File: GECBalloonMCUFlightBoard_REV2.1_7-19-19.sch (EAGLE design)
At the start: 59 parts, among them IC1 PIC32MX360F512L, Q1 IRF3704L-V, Q2 IRF3704L-V, U1 ADS1118, U2 ADS1118, X2 MALE_VGA, Y1 SG-636PCW_50.0000MC3__ROHS

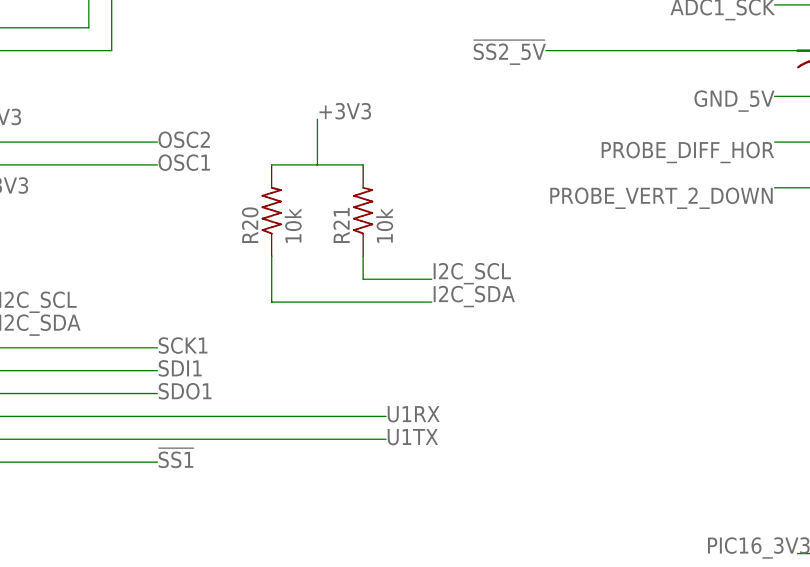
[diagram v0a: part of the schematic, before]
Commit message: Renamed board files to represent the current date and revision. Also archived the version of the board sent out in the OldBoardRevisions folder
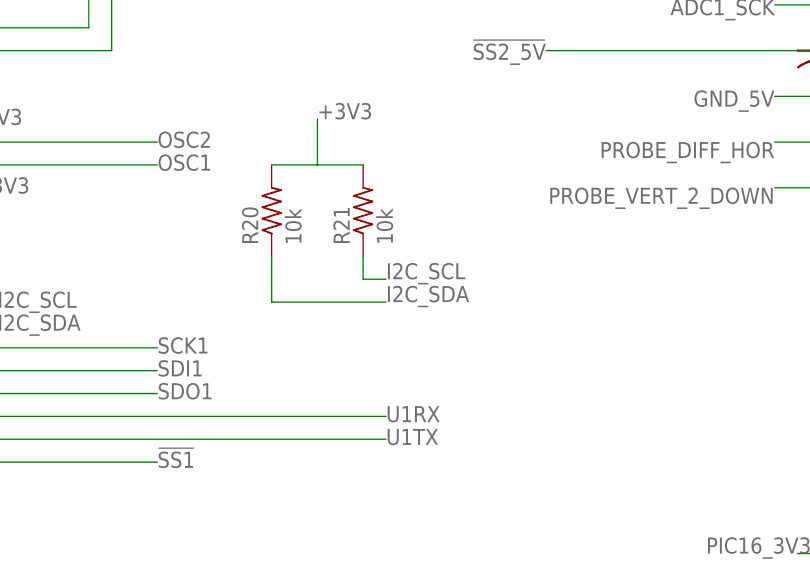
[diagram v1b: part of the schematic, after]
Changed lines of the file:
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@@
 <pinref part="R21" gate="G$1" pin="1"/>
 <wire x1="175.26" y1="50.8" x2="175.26" y2="48.26" width="0.1524" layer="91"/>
-<wire x1="175.26" y1="48.26" x2="182.88" y2="48.26" width="0.1524" layer="91"/>
-<label x="182.88" y="48.26" size="1.778" layer="95"/>
+<wire x1="175.26" y1="48.26" x2="177.8" y2="48.26" width="0.1524" layer="91"/>
+<label x="177.8" y="48.26" size="1.778" layer="95"/>
 </segment>
 </net>
@@
 <pinref part="R20" gate="G$1" pin="1"/>
 <wire x1="165.1" y1="50.8" x2="165.1" y2="45.72" width="0.1524" layer="91"/>
-<wire x1="165.1" y1="45.72" x2="182.88" y2="45.72" width="0.1524" layer="91"/>
-<label x="182.88" y="45.72" size="1.778" layer="95"/>
+<wire x1="165.1" y1="45.72" x2="177.8" y2="45.72" width="0.1524" layer="91"/>
+<label x="177.8" y="45.72" size="1.778" layer="95"/>
 </segment>
 </net>
